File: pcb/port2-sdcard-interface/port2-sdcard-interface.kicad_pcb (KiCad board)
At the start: 4 copper layers, 80 x 100 mm, 58 parts, among them J2 P2000T Port 2, J3 SD Card, U1 CY62128ELL-45SXI, U10 74HC32, U11 74HC273, U12 74HC165, U13 74HC595, U14 74HC00, U15 SST39SF010, U17 74HC138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

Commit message: Adding CRC16 check for monitor and shuffling routines
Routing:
- net VCC: track 193.7 -> 194.3 mm
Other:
- board text added: "(bank)"
- board text added: "(led)"
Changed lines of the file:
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@@
     (property "ki_keywords" "TTL DFF")
     (attr smd)
-    (fp_text reference "U3" (at 0 5.28 90) (layer "B.SilkS")
+    (fp_text reference "U3" (at 4.618 -3.2 -180) (layer "B.SilkS")
         (effects (font (size 1 1) (thickness 0.15)) (justify mirror))
     )
@@
     (effects (font (size 1 1) (thickness 0.15)) (justify left bottom mirror))
   )
+  (gr_text "(bank)" (at 100.255 61.63 90) (layer "B.SilkS")
+    (effects (font (size 0.7 0.7) (thickness 0.1)) (justify left bottom mirror))
+  )
   (gr_text "A-SIDE\nBACK" (at 96.2101 104.9022) (layer "B.SilkS")
     (effects (font (size 1.5 1.5) (thickness 0.3)) (justify mirror))
@@
     (effects (font (size 0.7 0.7) (thickness 0.1)) (justify left bottom mirror))
   )
+  (gr_text "(led)" (at 88.855 39.43) (layer "B.SilkS")
+    (effects (font (size 0.7 0.7) (thickness 0.1)) (justify left bottom mirror))
+  )
   (gr_text "2a" (at 37.7497 106.6421) (layer "B.SilkS")
     (effects (font (size 1 1) (thickness 0.15)) (justify mirror))
@@
   (via (at 93.199 58.66) (size 0.8) (drill 0.4) (layers "F.Cu" "B.Cu") (net 1))
   (via (at 33.763 101.078) (size 0.8) (drill 0.4) (layers "F.Cu" "B.Cu") (net 1))
-  (via (at 99.6081 65.3785) (size 0.8) (drill 0.4) (layers "F.Cu" "B.Cu") (net 1))
+  (via (at 99.855 66.03) (size 0.8) (drill 0.4) (layers "F.Cu" "B.Cu") (net 1))
   (via (at 84.055 39.5601) (size 0.8) (drill 0.4) (layers "F.Cu" "B.Cu") (net 1))
   (via (at 74.657 97.522) (size 0.8) (drill 0.4) (layers "F.Cu" "B.Cu") (net 1))
@@
   (segment (start 76.435 84.865) (end 78.764 84.865) (width 0.25) (layer "B.Cu") (net 1))
   (segment (start 34.525 52.734) (end 36.981 52.734) (width 0.25) (layer "B.Cu") (net 1))
-  (segment (start 99.6081 65.3785) (end 98.3935 65.3785) (width 0.25) (layer "B.Cu") (net 1))
   (segment (start 76.435 64.545) (end 78.51 64.545) (width 0.25) (layer "B.Cu") (net 1))
   (segment (start 31.731 38.34) (end 33.806 40.415) (width 0.25) (layer "B.Cu") (net 1))
@@
   (segment (start 51.035 50.575) (end 53.364 50.575) (width 0.25) (layer "B.Cu") (net 1))
   (segment (start 86.595 56.12) (end 86.595 54.5422) (width 0.25) (layer "B.Cu") (net 1))
+  (segment (start 99.6081 65.9831) (end 99.655 66.03) (width 0.25) (layer "B.Cu") (net 1))
   (segment (start 51.035 40.6475) (end 51.035 42.15) (width 0.25) (layer "B.Cu") (net 1))
   (segment (start 49.225 46.595) (end 50.654 46.595) (width 0.25) (layer "B.Cu") (net 1))
@@
   (segment (start 78.975 85.076) (end 78.975 86.6) (width 0.25) (layer "B.Cu") (net 1))
   (segment (start 34.525 92.485) (end 34.525 93.966) (width 0.25) (layer "B.Cu") (net 1))
+  (segment (start 98.025 65.01) (end 98.835 65.01) (width 0.25) (layer "B.Cu") (net 1))
   (segment (start 25.889 52.945) (end 25.889 55.104) (width 0.25) (layer "B.Cu") (net 1))
   (segment (start 34.525 75.975) (end 34.525 77.456) (width 0.25) (layer "B.Cu") (net 1))
@@
   (segment (start 37.065 76.694) (end 37.065 80.25) (width 0.25) (layer "B.Cu") (net 1))
   (segment (start 61.195 77.202) (end 61.195 78.98) (width 0.25) (layer "B.Cu") (net 1))
-  (segment (start 98.3935 65.3785) (end 98.025 65.01) (width 0.25) (layer "B.Cu") (net 1))
   (segment (start 36.346 75.975) (end 37.065 76.694) (width 0.25) (layer "B.Cu") (net 1))
   (segment (start 76.435 95.025) (end 78.764 95.025) (width 0.25) (layer "B.Cu") (net 1))
@@
   (segment (start 38.335 64.756) (end 38.335 66.15) (width 0.25) (layer "B.Cu") (net 1))
   (segment (start 76.435 74.57) (end 78.629 74.57) (width 0.25) (layer "B.Cu") (net 1))
+  (segment (start 98.835 65.01) (end 99.855 66.03) (width 0.25) (layer "B.Cu") (net 1))
   (segment (start 76.435 84.865) (end 76.435 86.6) (width 0.25) (layer "B.Cu") (net 1))
   (segment (start 25.889 52.945) (end 24.492 52.945) (width 0.25) (layer "B.Cu") (net 1))
@@
   (segment (start 99.3008 76.7639) (end 99.3008 74.1065) (width 0.25) (layer "B.Cu") (net 103))
   (segment (start 97.96 77.71) (end 98.3547 77.71) (width 0.25) (layer "B.Cu") (net 103))
-  (segment (start 97.96 80.25) (end 98.0199 80.3099) (width 0.25) (layer "B.Cu") (net 104))
-  (segment (start 100.3406 65.0807) (end 98.9999 63.74) (width 0.25) (layer "B.Cu") (net 104))
-  (segment (start 98.0199 80.3099) (end 99.7443 80.3099) (width 0.25) (layer "B.Cu") (net 104))
-  (segment (start 98.9999 63.74) (end 98.025 63.74) (width 0.25) (layer "B.Cu") (net 104))
-  (segment (start 99.7443 80.3099) (end 100.3406 79.7136) (width 0.25) (layer "B.Cu") (net 104))
-  (segment (start 100.3406 79.7136) (end 100.3406 65.0807) (width 0.25) (layer "B.Cu") (net 104))
+  (segment (start 98.0199 80.3099) (end 97.96 80.25) (width 0.25) (layer "B.Cu") (net 104))
+  (segment (start 100.58 65.3201) (end 100.58 79.4742) (width 0.25) (layer "B.Cu") (net 104))
+  (segment (start 100.58 79.4742) (end 99.7443 80.3099) (width 0.25) (layer "B.Cu") (net 104))
+  (segment (start 99.7443 80.3099) (end 98.0199 80.3099) (width 0.25) (layer "B.Cu") (net 104))
+  (segment (start 98.9999 63.74) (end 100.58 65.3201) (width 0.25) (layer "B.Cu") (net 104))
+  (segment (start 98.025 63.74) (end 98.9999 63.74) (width 0.25) (layer "B.Cu") (net 104))
   (segment (start 93.4583 65.01) (end 93.075 65.01) (width 0.25) (layer "B.Cu") (net 107))
   (segment (start 94.3897 65.9414) (end 93.4583 65.01) (width 0.25) (layer "B.Cu") (net 107))

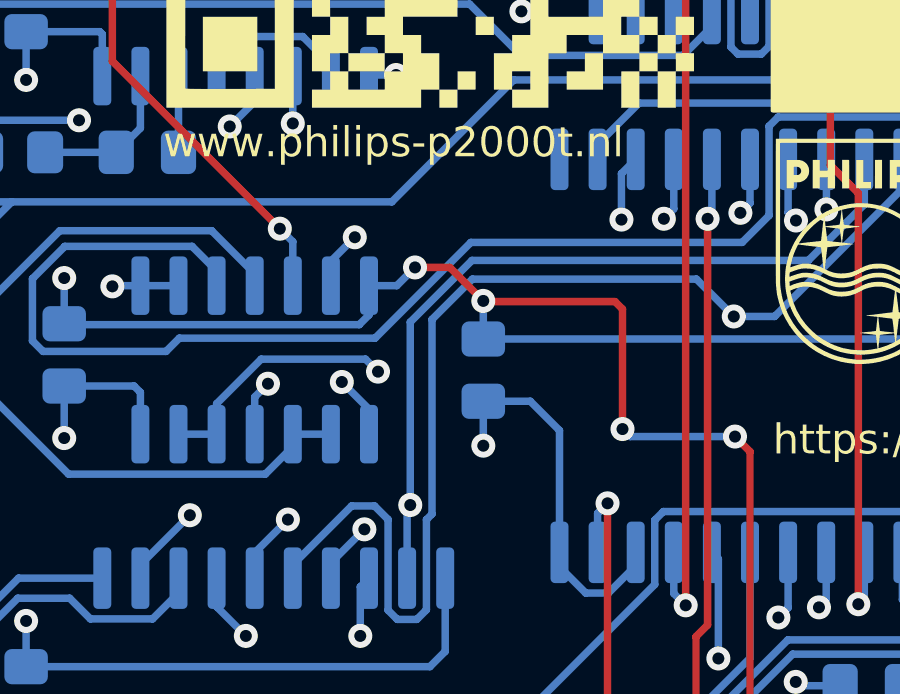
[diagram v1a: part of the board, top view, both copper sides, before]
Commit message: Adding OSHW logo
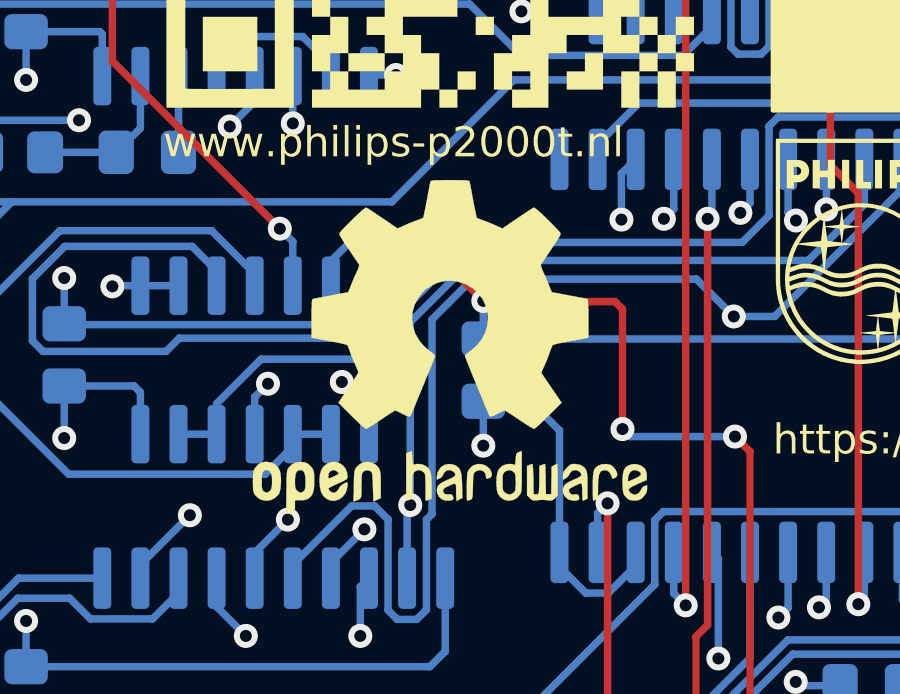
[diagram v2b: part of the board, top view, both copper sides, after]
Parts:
- added REF**: OSHW-Logo2_14.6x12mm_SilkScreen, Symbol:OSHW-Logo2_14.6x12mm_SilkScreen, F.Cu at (48.7, 63.2)
